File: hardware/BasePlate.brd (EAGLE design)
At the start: 292.2 x 120 mm, 5 parts

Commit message: consolidate RemoteParts libraries
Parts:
- E$3, E$4: device RemotePartsA:FRSKY-TARANIS-GIMBAL -> RemoteParts:FRSKY-TARANIS-GIMBAL
- E$5: device RemotePartsA:SPARKFUN_LCD_33 -> RemoteParts:SPARKFUN_LCD_33
- E$6: device RemotePartsA:CONTROLLER_OUTLINE -> RemoteParts:CONTROLLER_OUTLINE
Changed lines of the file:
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@@
 </autorouter>
 <elements>
-<element name="E$3" library="RemotePartsA" package="FRSKY-TARANIS-GIMBAL" value="" x="-108" y="0" locked="yes"/>
-<element name="E$4" library="RemotePartsA" package="FRSKY-TARANIS-GIMBAL" value="" x="108" y="0" locked="yes" rot="R180"/>
-<element name="E$5" library="RemotePartsA" package="SPARKFUN_LCD_33" value="" x="-40" y="-53" locked="yes"/>
-<element name="E$6" library="RemotePartsA" package="CONTROLLER_OUTLINE" value="" x="0" y="0" locked="yes"/>
+<element name="E$3" library="RemoteParts" package="FRSKY-TARANIS-GIMBAL" value="" x="-108" y="0" locked="yes"/>
+<element name="E$4" library="RemoteParts" package="FRSKY-TARANIS-GIMBAL" value="" x="108" y="0" locked="yes" rot="R180"/>
+<element name="E$5" library="RemoteParts" package="SPARKFUN_LCD_33" value="" x="-40" y="-53" locked="yes"/>
+<element name="E$6" library="RemoteParts" package="CONTROLLER_OUTLINE" value="" x="0" y="0" locked="yes"/>
 <element name="E$7" library="BOBs" package="ATMEGA128RFA1" value="" x="-25.5" y="58.5" locked="yes" rot="R270"/>
 </elements>

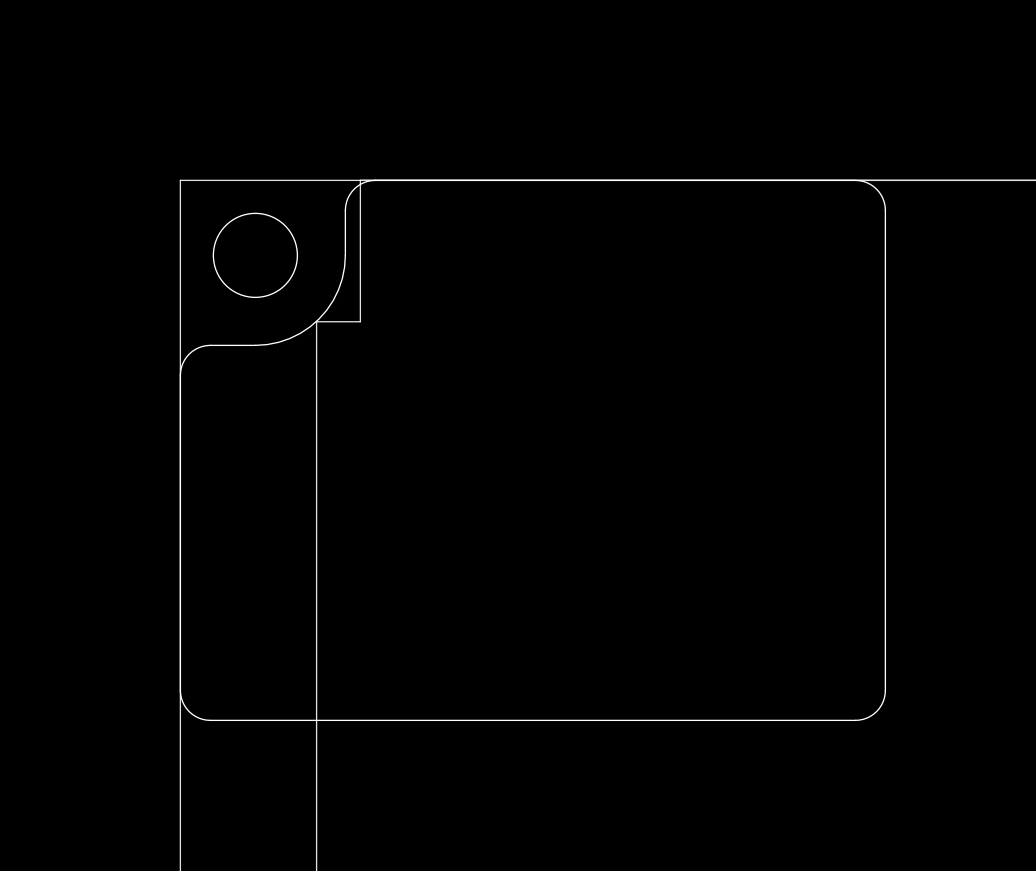
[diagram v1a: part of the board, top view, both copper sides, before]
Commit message: description of fix for receive problem
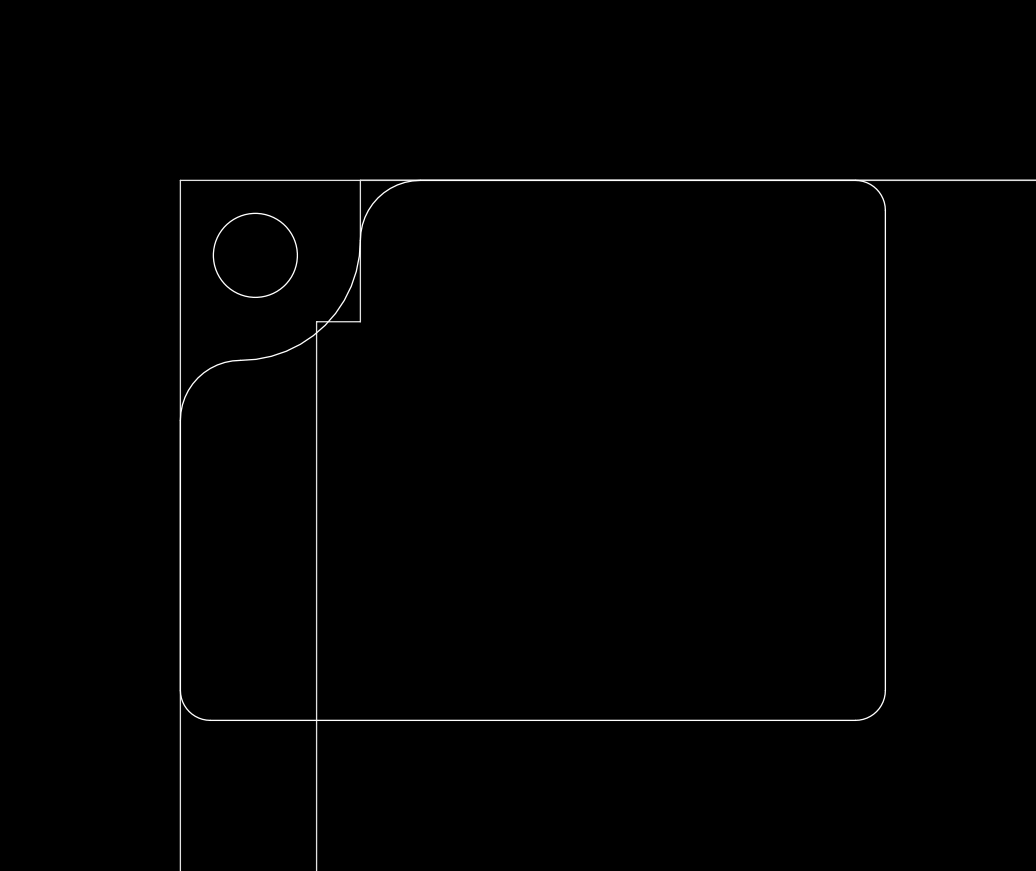
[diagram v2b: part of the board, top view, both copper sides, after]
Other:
- outline, holes or cut-outs redrawn
- board text added: "TODO: * remove cutout for removing redboard."
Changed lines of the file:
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@@
 <wire x1="85" y1="25" x2="83" y2="23" width="0.0254" layer="20" curve="-90"/>
 <wire x1="-14" y1="-5" x2="-19" y2="0" width="0.0254" layer="20" curve="90"/>
-<wire x1="-40" y1="-34" x2="-40" y2="-23.5" width="0.0254" layer="20"/>
-<wire x1="-40" y1="-23.5" x2="-39" y2="-22.5" width="0.0254" layer="20" curve="-90"/>
-<wire x1="-39" y1="-22.5" x2="-37.5" y2="-22.5" width="0.0254" layer="20"/>
-<wire x1="-37.5" y1="-22.5" x2="-34.5" y2="-19.5" width="0.0254" layer="20" curve="90"/>
-<wire x1="-34.5" y1="-19.5" x2="-34.5" y2="-18" width="0.0254" layer="20"/>
-<wire x1="-34.5" y1="-18" x2="-33.5" y2="-17" width="0.0254" layer="20" curve="-90"/>
-<wire x1="-33.5" y1="-17" x2="-17.5" y2="-17" width="0.0254" layer="20"/>
+<wire x1="-40" y1="-34" x2="-40" y2="-25" width="0.0254" layer="20"/>
+<wire x1="-40" y1="-25" x2="-38" y2="-23" width="0.0254" layer="20" curve="-90"/>
+<wire x1="-38" y1="-23" x2="-34" y2="-19" width="0.0254" layer="20" curve="90"/>
+<wire x1="-34" y1="-19" x2="-32" y2="-17" width="0.0254" layer="20" curve="-90"/>
+<wire x1="-32" y1="-17" x2="-17.5" y2="-17" width="0.0254" layer="20"/>
 <wire x1="-17.5" y1="-17" x2="-16.5" y2="-18" width="0.0254" layer="20" curve="-90"/>
 <wire x1="-16.5" y1="-18" x2="-16.5" y2="-34" width="0.0254" layer="20"/>
@@
 <wire x1="-17.5" y1="-35" x2="-39" y2="-35" width="0.0254" layer="20"/>
 <wire x1="-39" y1="-35" x2="-40" y2="-34" width="0.0254" layer="20" curve="-90"/>
+<text x="-135" y="74.5" size="1.778" layer="48">TODO:
+* remove cutout for removing redboard.</text>
 </plain>
 <attributes>
@@
 </board>
 </drawing>
+<compatibility>
+<note version="6.3" minversion="6.2.2" severity="warning">
+Since Version 6.2.2 text objects can contain more than one line,
+which will not be processed correctly with this version.
+</note>
+</compatibility>
 </eagle>
